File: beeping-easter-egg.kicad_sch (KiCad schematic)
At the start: 9 parts, among them Q1 2N3904, SW1 SW_SPDT_312, U1 ICM7556

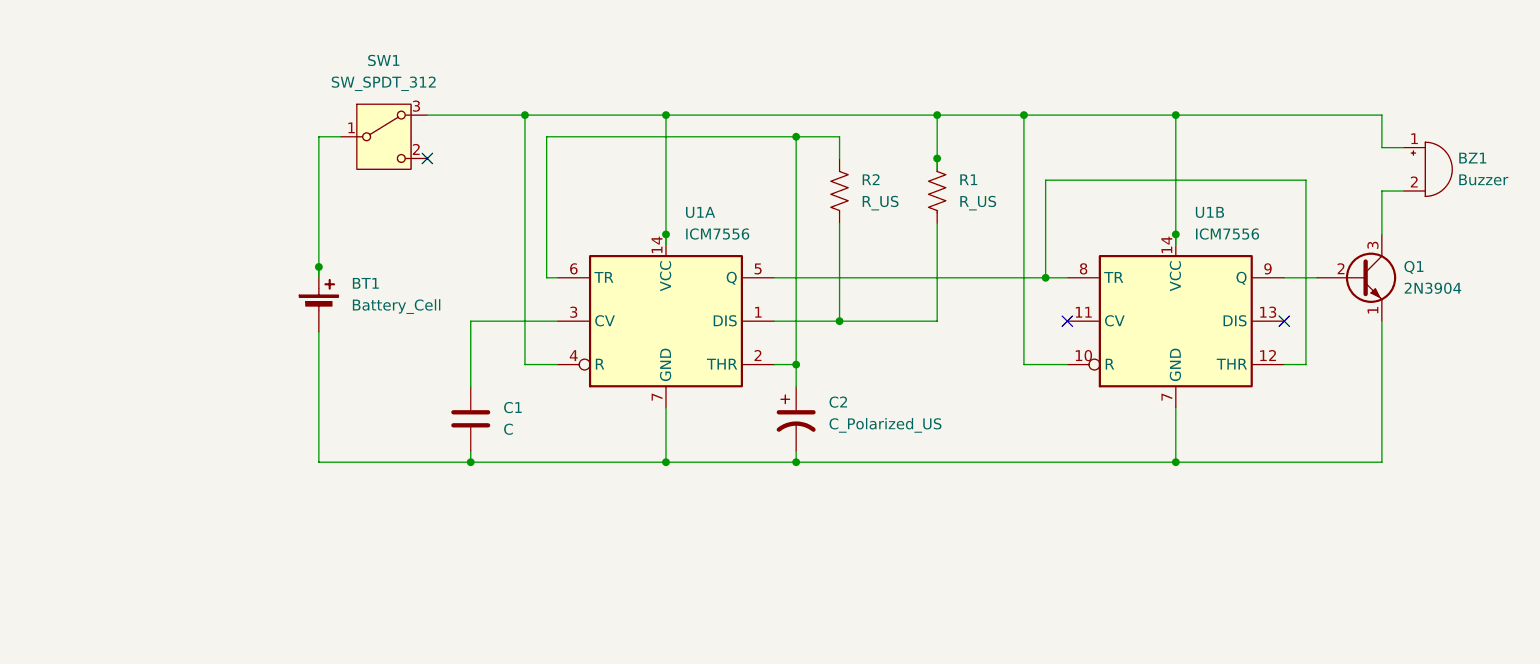
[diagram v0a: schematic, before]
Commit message: Change buzzer driver to pnp, remove 555 inverting buffer.
Add reverse polarity protection.
Add custom footprint for battery holder.
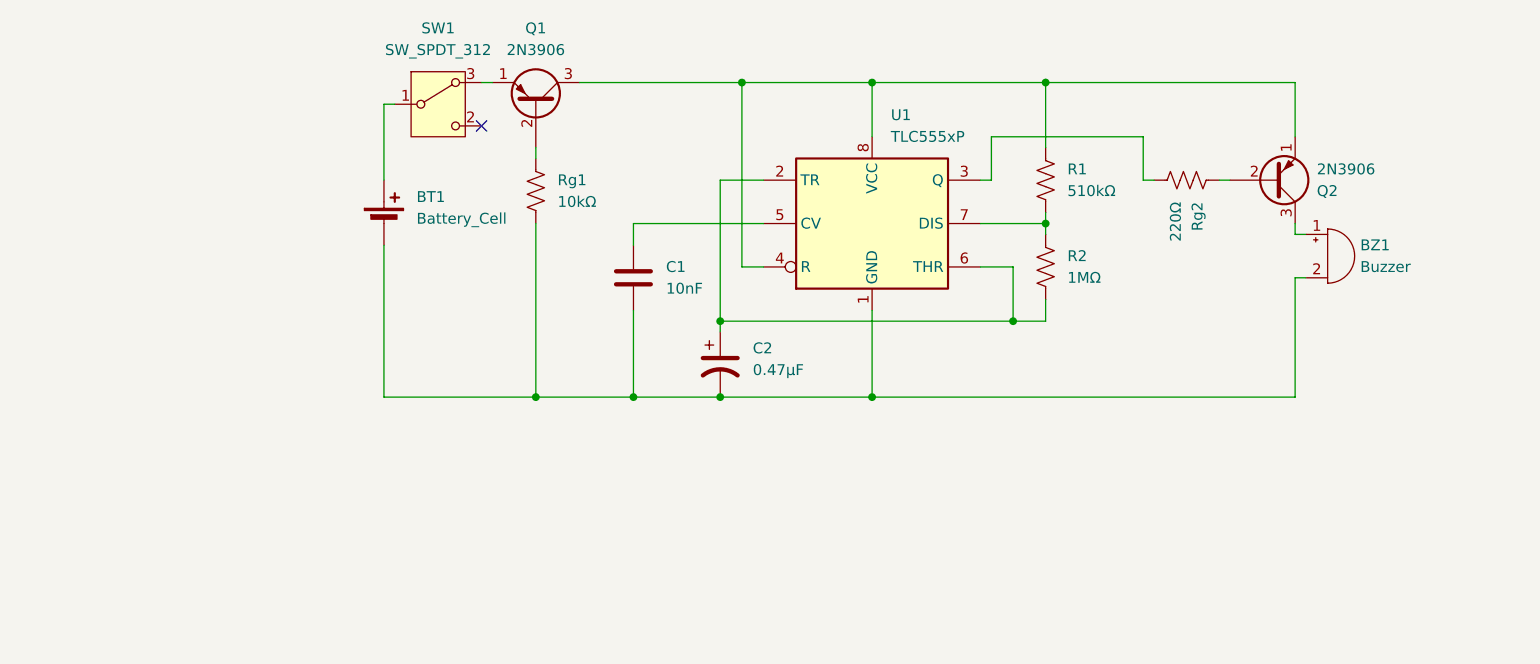
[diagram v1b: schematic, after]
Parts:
- removed Q1: 2N3904, Package_TO_SOT_THT:TO-92_Inline, symbol Transistor_BJT:2N3904
- removed U1: ICM7556, Package_DIP:DIP-14_W7.62mm, symbol Timer:ICM7556
- added Q1, Q2: 2N3906, Package_TO_SOT_THT:TO-92_Inline, symbol Transistor_BJT:2N3906
- added Rg1: 10kΩ, Resistor_THT:R_Axial_DIN0207_L6.3mm_D2.5mm_P7.62mm_Horizontal, symbol Device:R_US
- added Rg2: 220Ω, Resistor_THT:R_Axial_DIN0207_L6.3mm_D2.5mm_P7.62mm_Horizontal, symbol Device:R_US
- added U1: TLC555xP, Package_DIP:DIP-8_W7.62mm, symbol Timer:TLC555xP
- BT1: footprint Battery:Battery_Panasonic_CR2032-HFN_Horizontal_CircularHoles -> Library:AAA-BAT-038-K01
- C1: value C -> 10nF
- C2: value C_Polarized_US -> 0.47µF
- R1: renamed from R2; value R_US -> 510kΩ
- R2: renamed from R1; value R_US -> 1MΩ
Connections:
- net at BT1.2 (-), C1.2, C2.2: now also BZ1.2 (-), Rg1.2, U1.1 (GND)
- net at R1.2: now also R2.1, U1.7 (DIS); no longer R2.2
- net at C1.1: now also U1.5 (CV)
- net at C2.1: now also R2.2, U1.2 (TR), U1.6 (THR); no longer R1.1
- new net: Q1.1 (E), SW1.3 (A)
- new net: BZ1.1 (+), Q2.3 (C)
- new net: Q1.2 (B), Rg1.1
- new net: Q1.3 (C), Q2.1 (E), R1.1, U1.4 (R), U1.8 (VCC)
- new net: Rg2.2, U1.3 (Q)
- new net: Q2.2 (B), Rg2.1
- no-connect marks 3 -> 1
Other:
- moved on the sheet: BT1, BZ1, C1, C2, R1, R2, SW1

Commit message: switch from bjts to mosfets
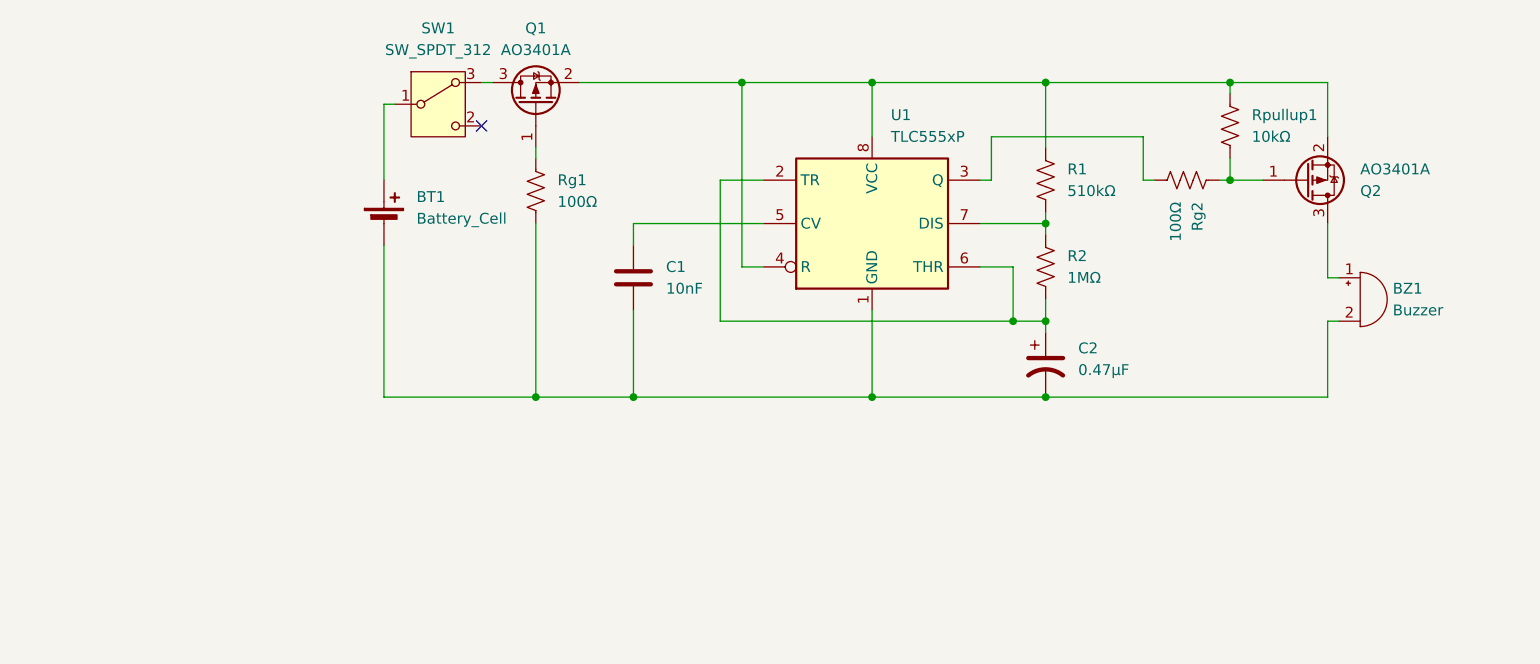
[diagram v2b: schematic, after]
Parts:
- removed Q1, Q2: 2N3906, Package_TO_SOT_THT:TO-92_Inline, symbol Transistor_BJT:2N3906
- added Q1, Q2: AO3401A, Package_TO_SOT_SMD:SOT-23, symbol Transistor_FET:AO3401A
- added Rpullup1: 10kΩ, Resistor_THT:R_Axial_DIN0207_L6.3mm_D2.5mm_P7.62mm_Horizontal, symbol Device:R_US
- Rg1: value 10kΩ -> 100Ω
- Rg2: value 220Ω -> 100Ω
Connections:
- net at SW1.3 (A): now also Q1.3 (D)
- net at BZ1.1 (+): now also Q2.3 (D)
- net at Rg1.1: now also Q1.1 (G)
- net at R1.1, U1.4 (R), U1.8 (VCC): now also Q1.2 (S), Q2.2 (S), Rpullup1.1
- net at Rg2.1: now also Q2.1 (G), Rpullup1.2
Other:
- moved on the sheet: BZ1, C2

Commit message: Switch to SMD footprints. Add filter cap to reset.
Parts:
- added C3: 10nF, Capacitor_SMD:C_0603_1608Metric, symbol Device:C
- BT1: footprint Library:AAA-BAT-038-K01 -> Battery:BatteryHolder_MYOUNG_BS-07-A1BJ001_CR2032
- C1: renamed from C2; footprint Capacitor_THT:CP_Radial_D5.0mm_P2.50mm -> Capacitor_SMD:C_0603_1608Metric
- C2: renamed from C1; footprint Capacitor_THT:CP_Radial_Tantal_D4.5mm_P2.50mm -> Capacitor_SMD:C_0603_1608Metric
- R1, R2, Rg1, Rpullup1: footprint Resistor_THT:R_Axial_DIN0207_L6.3mm_D2.5mm_P7.62mm_Horizontal -> Resistor_SMD:R_0603_1608Metric
- Rg2: value 100Ω -> 300Ω; footprint Resistor_THT:R_Axial_DIN0207_L6.3mm_D2.5mm_P7.62mm_Horizontal -> Resistor_SMD:R_0603_1608Metric
- U1: footprint Package_DIP:DIP-8_W7.62mm -> Package_SO:SOIC-8_3.9x4.9mm_P1.27mm
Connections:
- net at Q1.2 (S), Q2.2 (S), R1.1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: now also C3.1
- net at BT1.2 (-), BZ1.2 (-), C1.2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: now also C3.2
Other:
- moved on the sheet: BT1, C2, Q1, Rg1, SW1

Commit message: Change 555 R and C values to reduce current. Ratio and thus timing stays the same. Some component renaming. Add LCSC field.
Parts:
- C1: value 0.47µF -> 0.047µF
- R1: value 510kΩ -> 5MΩ
- R2: value 1MΩ -> 10MΩ
- renumbered Rg1 to R3, Rg2 to R4, Rpullup1 to R5
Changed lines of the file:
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@@
 			)
 		)
-		(property "Value" "1MΩ"
+		(property "Value" "10MΩ"
 			(at 162.56 69.8499 0)
 			(effects
@@
 			)
 		)
-		(property "Value" "0.47µF"
+		(property "Value" "0.047µF"
 			(at 163.83 80.6449 0)
 			(effects
@@
 		(on_board yes)
 		(dnp no)
-		(property "Reference" "Rg1"
+		(property "Reference" "R3"
 			(at 99.06 58.4199 0)
 			(effects
@@
 			(project "beeping-easter-egg"
 				(path "/d8933e53-1592-4685-95eb-2622e257800f"
-					(reference "Rg1")
+					(reference "R3")
 					(unit 1)
 				)
@@
 		(on_board yes)
 		(dnp no)
-		(property "Reference" "Rpullup1"
+		(property "Reference" "R5"
 			(at 184.15 50.7999 0)
 			(effects
@@
 			(project "beeping-easter-egg"
 				(path "/d8933e53-1592-4685-95eb-2622e257800f"
-					(reference "Rpullup1")
+					(reference "R5")
 					(unit 1)
 				)
@@
 			)
 		)
-		(property "Value" "510kΩ"
+		(property "Value" "5MΩ"
 			(at 162.56 59.6899 0)
 			(effects
@@
 		(on_board yes)
 		(dnp no)
-		(property "Reference" "Rg2"
+		(property "Reference" "R4"
 			(at 177.8001 60.96 0)
 			(effects
@@
 			(project "beeping-easter-egg"
 				(path "/d8933e53-1592-4685-95eb-2622e257800f"
-					(reference "Rg2")
-					(unit 1)
-				)
+					(reference "R4")
+					(unit 1)
+				)

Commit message: Adjust R1 value to nearest commonly availably value. Add LCSC number for battery holder.
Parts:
- R1: value 5MΩ -> 5.1MΩ
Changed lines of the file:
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@@
 			)
 		)
-		(property "Value" "5MΩ"
+		(property "Value" "5.1MΩ"
 			(at 162.56 59.6899 0)
 			(effects

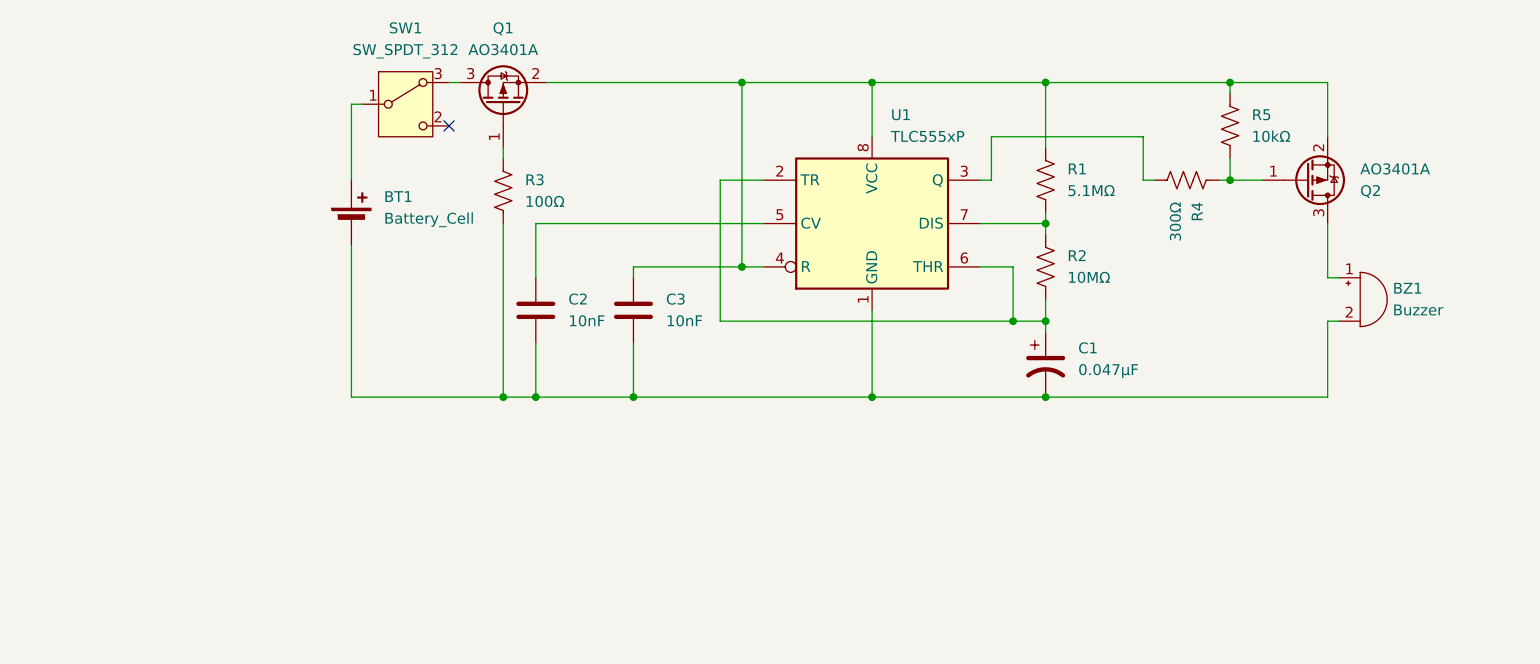
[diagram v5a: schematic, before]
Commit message: Convert to kicad version 9. Add LCSC part numbers.
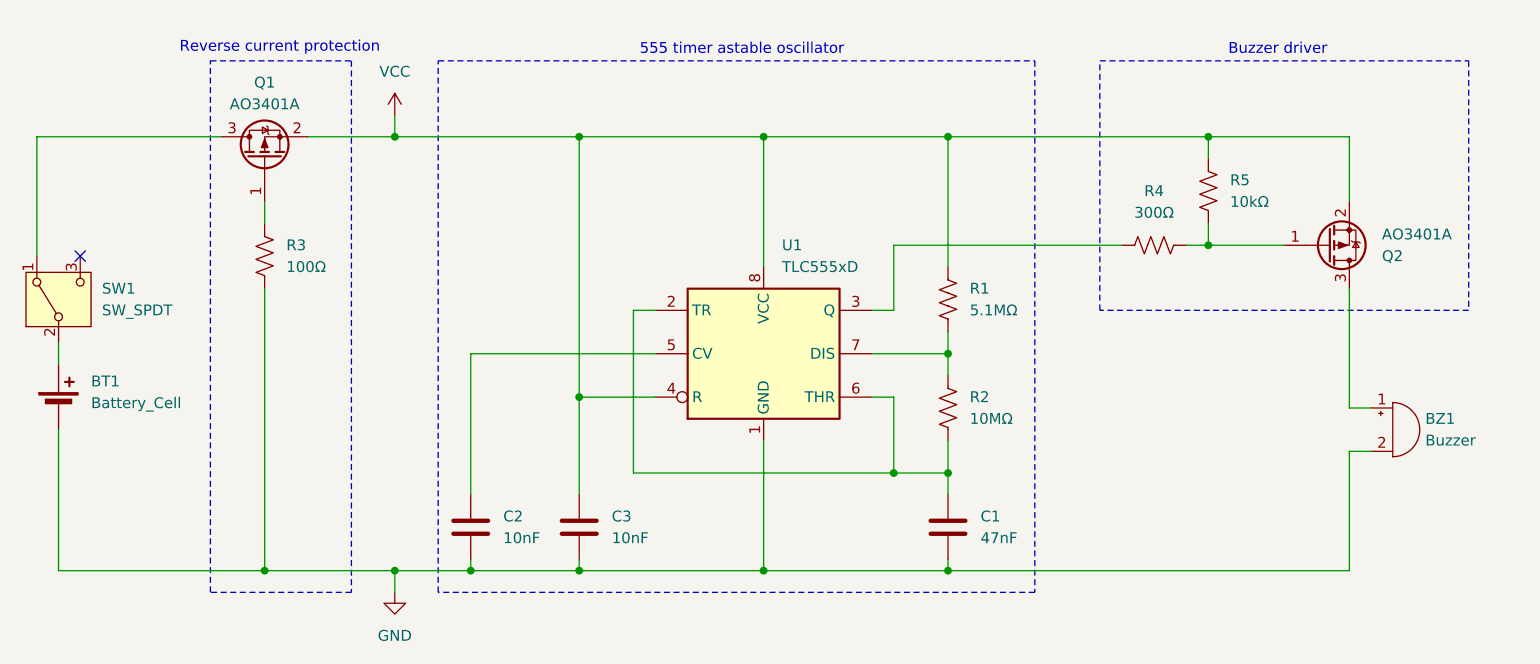
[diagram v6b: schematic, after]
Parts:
- removed C1: 0.047µF, Capacitor_SMD:C_0603_1608Metric, symbol Device:C_Polarized_US
- removed SW1: SW_SPDT_312, Connector_PinHeader_2.54mm:PinHeader_1x03_P2.54mm_Vertical, symbol Switch:SW_SPDT_312
- removed U1: TLC555xP, Package_SO:SOIC-8_3.9x4.9mm_P1.27mm, symbol Timer:TLC555xP
- added C1: 47nF, Capacitor_SMD:C_0603_1608Metric, symbol Device:C
- added SW1: SW_SPDT, symbol Switch:SW_SPDT
- added U1: TLC555xD, Package_SO:SOIC-8_3.9x4.9mm_P1.27mm, symbol Timer:TLC555xD
- BT1: footprint Battery:BatteryHolder_MYOUNG_BS-07-A1BJ001_CR2032 -> (none); LCSC (none) -> C964750
- BZ1: LCSC (none) -> C96222
- C2, C3: LCSC (none) -> C57112
- Q1, Q2: LCSC (none) -> C15127
- R1: LCSC (none) -> C13320
- R2: LCSC (none) -> C7250
- R3: LCSC (none) -> C22775
- R4: LCSC (none) -> C23025
- R5: LCSC (none) -> C25804
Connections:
- net at R1.2, R2.1: now also U1.7 (DIS)
- net at R2.2: now also C1.1, U1.2 (TR), U1.6 (THR)
- net at Q2.1 (G), R5.2: now also R4.2; no longer R4.1
- net VCC: now reaches C3.1, Q1.2 (S), Q2.2 (S), R1.1, R5.1
- net VCC: now also U1.4 (R), U1.8 (VCC)
- net at BT1.1 (+): now also SW1.2 (B)
- net at Q1.3 (D): now also SW1.1 (A)
- net GND: now reaches BT1.2 (-), BZ1.2 (-), C2.2, C3.2, R3.2
- net GND: now also C1.2, U1.1 (GND)
- net at C2.1: now also U1.5 (CV)
- new net: R4.1, U1.3 (Q)
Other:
- note added: "555 timer astable oscillator"
- note added: "Buzzer driver"
- note added: "Reverse current protection"
